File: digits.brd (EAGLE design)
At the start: 240.9 x 81 mm, 49 parts, among them IC1 STP16CP05 / STP16CPC26, IC2 STP16CP05 / STP16CPC26, IC3 ATMEGA32U4QFN, IC4 ATMEGA32U4TQFP-44, J1 POWER_JACKPTH_LOCK, J2 ACCESSORY, X1 CRYSTALHC49

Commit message: added boost converter
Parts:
- added C11, C12: 0.1uF, SparkFun-Capacitors:0805
- added C13: 100uF, SparkFun-Capacitors:PANASONIC_D
- added C14: 470uF, SparkFun-Capacitors:PANASONIC_D
- added C15: 470pF, SparkFun-Capacitors:0805
- added D3: BYV10-40, diode:MELF-MLL41
- added IC6: 7805DT, adafruit:TO252
- added L2: 200uH, Livestream:SRN1060
- added R13: 0.33R, SparkFun-Resistors:0805
- added R14: 1.2k, SparkFun-Resistors:0805
- added R15: 3.6k, SparkFun-Resistors:0805
- added U1: MC34063SMD, SparkFun-PowerIC:SO08
- C7, C8, C9: value 100nF -> 0.1uF
- moved J2 85.1 mm to (124.5, 100.8)
- moved U$1 48.0 mm to (69.5, 30.1)
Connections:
- removed net D13: J2.18
- removed net MOSI: IC1.2, JP3.3
- removed net PD0: JP3.7, JP6.4
- removed net PD1: JP3.8, JP6.3
- removed net SCK: IC1.3, IC2.3, JP3.4, JP6.7
- new net N$13: R13.1, U1.1, U1.7, U1.8
- new net N$14: D3.C, L2.P$1, U1.2
- new net N$15: C15.2, U1.3
- new net N$16: R14.2, R15.1, U1.5
- new net VCCLEDS: C14.+, L2.P$2, R15.2, T1.2, T2.2, T3.2, T4.2, T5.2
- net BLANK: no longer JP3.6, JP6.5
- net D0/RX: now also JP3.3, JP6.8
- net D1/TX: now also JP3.4, JP6.7
- net D2/SDA: now also JP3.5, JP6.6
- net D3/SCL: now also JP3.6, JP6.5
- net D4/MOSI: now also IC1.2
- net D6/SCK: now also IC1.3, IC2.3
- net D7: now also JP3.7, JP6.4
- net D8: now also JP3.8, JP6.3
- net GND: now also C11.2, C12.2, C13.-, C14.-, C15.1, D3.A, IC6.3, R14.1, U1.4
- net LATCH: no longer JP3.5, JP6.6
- net SDO2: no longer JP6.8
- net VCC: now also C13.+, R13.2, U1.6; no longer C1.1, C2.1, IC1.24, IC2.24, J2.1, J2.2, JP3.1, JP3.2, JP6.10, JP6.9, T1.2, T2.2, T3.2, T4.2, T5.2
- net VCC5V: now also C1.1, C12.1, C2.1, IC1.24, IC2.24, IC6.2, J2.1, J2.2, JP3.1, JP6.10
- net VCC9V: now also C11.1, IC6.1, JP3.2, JP6.9
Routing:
- net VCC: track 572.5 -> 0.00 mm, vias 10 -> 0
- net VCC5V: track 71.9 -> 621.6 mm, vias 6 -> 16
- net BLANK: track 347.1 -> 17.3 mm, vias 6 -> 1
- net PD0: track 265.0 -> 0.00 mm, vias 9 -> 0
- net PD1: track 240.4 -> 0.00 mm, vias 3 -> 0
- net LATCH: track 306.4 -> 66.6 mm, vias 8 -> 3
- net SCK: track 210.4 -> 0.00 mm, vias 7 -> 0
- net MOSI: track 140.8 -> 0.00 mm, vias 6 -> 0
- net D13: track 112.6 -> 0.00 mm, vias 3 -> 0
- net D7: track 96.0 -> 194.7 mm, vias 1 -> 5
- net D9: track 101.2 -> 8.00 mm, vias 3 -> 0
- net D5/MISO: track 127.5 -> 53.2 mm, vias 2 -> 1
- net D12: track 65.7 -> 2.91 mm, vias 2 -> 0
- net D11: track 64.4 -> 6.59 mm, vias 4 -> 2
- net D1/TX: track 61.3 -> 10.6 mm, vias 2 -> 0
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
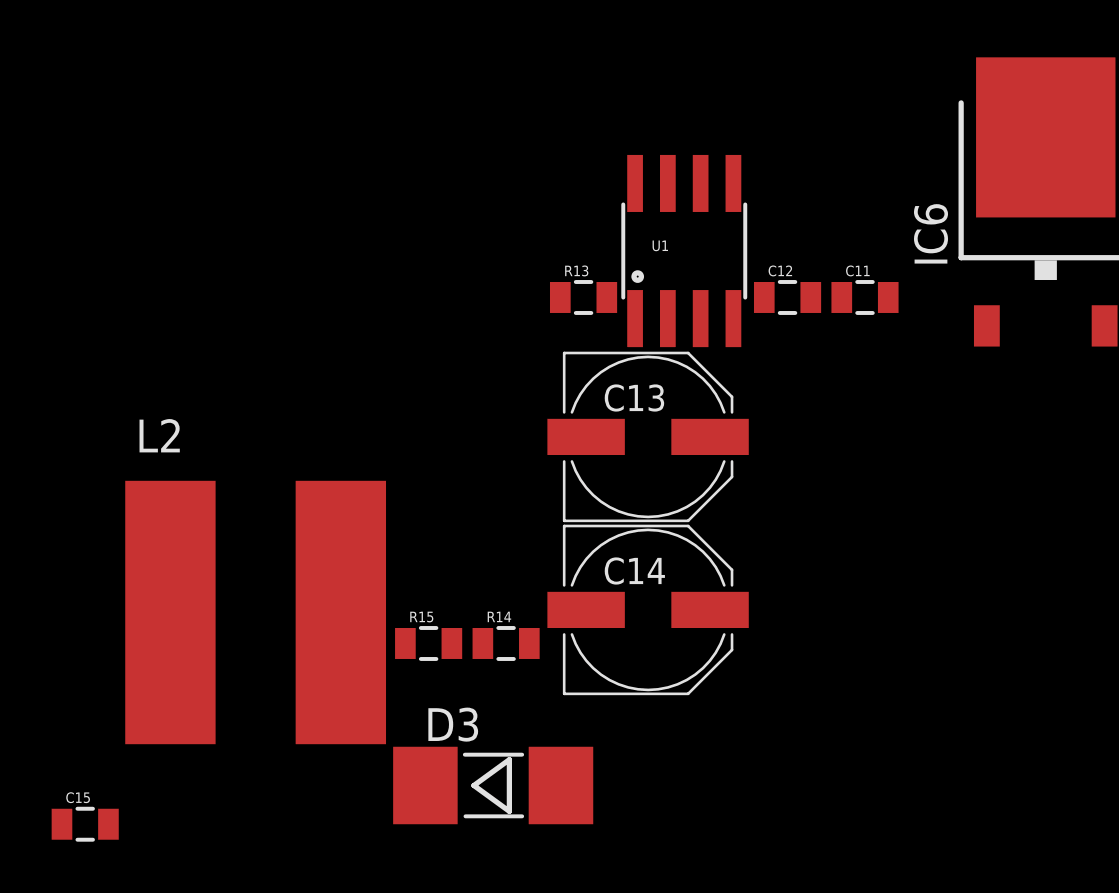
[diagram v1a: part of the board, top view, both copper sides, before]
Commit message: added tssop shifter, pololu boost
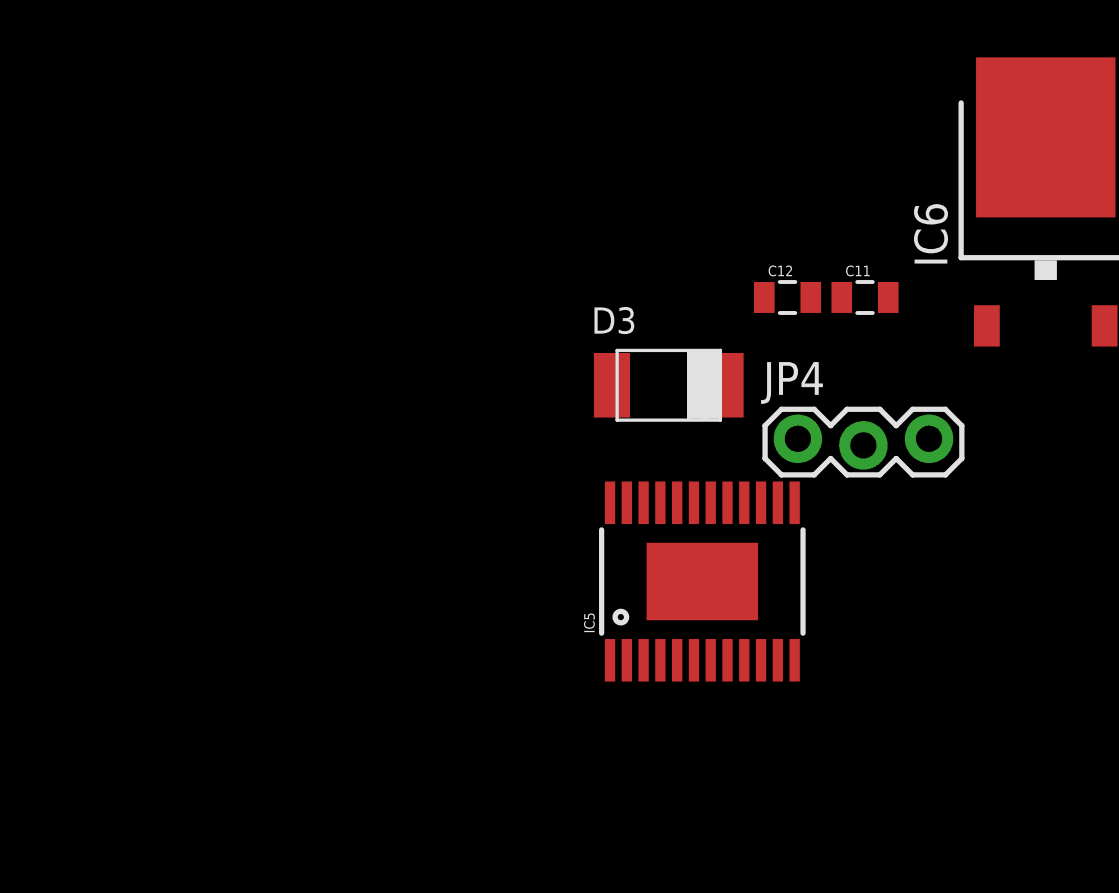
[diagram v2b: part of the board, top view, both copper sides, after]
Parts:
- removed C13: 100uF, SparkFun-Capacitors:PANASONIC_D
- removed C14: 470uF, SparkFun-Capacitors:PANASONIC_D
- removed C15: 470pF, SparkFun-Capacitors:0805
- removed L2: 200uH, Livestream:SRN1060
- removed R13: 0.33R, SparkFun-Resistors:0805
- removed R14: 1.2k, SparkFun-Resistors:0805
- removed R15: 3.6k, SparkFun-Resistors:0805
- removed U1: MC34063SMD, SparkFun-PowerIC:SO08
- added IC5: STP16CP05, digits:TSSOP-24
- added JP4: (no value), SparkFun-Connectors:1X03_LOCK
- D3: value BYV10-40 -> PMEG3030EP; device diode:MELF-MLL41 -> digits:SOD-128
- moved D3 16.9 mm to (-47.1, -6.40)
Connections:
- removed net N$14: D3.C, L2.P$1, U1.2
- removed net N$15: C15.2, U1.3
- removed net N$16: R14.2, R15.1, U1.5
- removed net VCC: C13.+, R13.2, U$1.24, U1.6
- removed net VCCLEDS: C14.+, L2.P$2, R15.2, T1.2, T2.2, T3.2, T4.2, T5.2
- net GND: now also JP4.2; no longer C13.-, C14.-, C15.1, D3.A, R14.1, U1.4
- net N$13: now also D3.A, JP4.3; no longer R13.1, U1.1, U1.7, U1.8
- net VCC5V: now also JP4.1
- net VCC9V: now also D3.C, T1.2, T2.2, T3.2, T4.2, T5.2, U$1.24

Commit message: started rerouting
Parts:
- removed IC5: STP16CP05, digits:TSSOP-24
- moved D3 95.5 mm to (44.6, 20.2), flipped to the bottom, turned to 90 degrees
- moved JP4 85.0 mm to (39.6, 14.8), flipped to the bottom, turned to 180 degrees
- moved T2 1.21 mm to (56.6, 5.50), turned to 270 degrees
- moved T3 1.20 mm to (105.7, 5.50), turned to 270 degrees
- moved T5 1.17 mm to (202.0, 5.50), turned to 270 degrees
- moved T4 1.08 mm to (153.6, 5.50), turned to 270 degrees
- moved T1 1.08 mm to (9.00, 5.40), turned to 270 degrees
- flipped C11 to the bottom
- flipped C12 to the bottom
- turned D1 to 180 degrees
- flipped IC6 to the bottom
- flipped R10 to the bottom
- flipped R11 to the bottom
- flipped R12 to the bottom
- flipped R7 to the bottom
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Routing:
- net VCC5V: track 621.6 -> 111.5 mm, vias 16 -> 6
- net D7: track 194.7 -> 50.1 mm, vias 5 -> 3
- net GATE3: track 163.3 -> 43.2 mm
- net GATE4: track 200.0 -> 81.0 mm
- net GATE2: track 118.3 -> 11.6 mm, vias 4 -> 2
- net VCC9V: track 0.00 -> 69.2 mm, vias 0 -> 1
- net ROW0: track 97.0 -> 41.3 mm
- net GATE1: track 65.2 -> 33.1 mm
- net GATE0: track 74.8 -> 64.9 mm
- net N$13: track 0.00 -> 3.36 mm
- net N$3: track 11.0 -> 13.2 mm

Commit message: layout, chronodot
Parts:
- added IC5: CHRONODOT, digits:CHRONODOT
- added R13, R14, R15, R16, R17: 910R, SparkFun-Resistors:0805
- added R18: 10k, SparkFun-Resistors:0805
- added SJ1: SOLDERJUMPERNO, SparkFun-Passives:SJ_2S-NO
- R10, R11, R12, R7, R9: value 1k -> 910R
- moved R12 212.0 mm to (198.4, 4.20), turned to 180 degrees
- moved R11 160.9 mm to (150.2, 4.50), turned to 180 degrees
- moved R10 109.9 mm to (102.1, 4.50), turned to 180 degrees
- moved J2 67.4 mm to (107.3, 35.6)
- moved R9 57.7 mm to (52.7, 4.50), turned to 180 degrees
- moved R7 10.1 mm to (5.40, 4.40), turned to 180 degrees
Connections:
- removed net D7/PRESENCE: IC3.33, IC4.33, J2.23, U$1.20
- removed net SDO2: IC2.22
- new net N$14: IC5.7, R18.2, SJ1.2
- new net PRESENCE: IC3.33, IC4.33, J2.23
- net D2/SDA: now also IC5.4
- net D3/SCL: now also IC5.3
- net D7: now also SJ1.1, U$1.20
- net GND: now also IC5.1
- net N$10: now also R14.1
- net N$11: now also R15.1
- net N$12: now also R17.1
- net N$8: now also R16.1
- net N$9: now also R13.1
- net VCC5V: now also IC5.2, R18.1
- net VCC9V: now also R13.2, R14.2, R15.2, R16.2, R17.2
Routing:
- net D7: track 50.1 -> 281.4 mm, vias 3 -> 10
- net VCC9V: track 69.2 -> 278.9 mm, vias 1 -> 10
- net D0/RX: track 0.00 -> 184.9 mm, vias 0 -> 3
- net D2/SDA: track 2.58 -> 176.0 mm, vias 0 -> 2
- net D3/SCL: track 0.00 -> 157.3 mm, vias 0 -> 5
- net D1/TX: track 10.6 -> 163.0 mm, vias 0 -> 2
- net GATE4: track 81.0 -> 229.1 mm, vias 4 -> 5
- net GATE3: track 43.2 -> 189.4 mm, vias 4 -> 2
- net LATCH: track 66.6 -> 187.9 mm, vias 3 -> 6
- net D9: track 8.00 -> 127.3 mm, vias 0 -> 4
- net BLANK: track 17.3 -> 135.7 mm, vias 1 -> 3
- net D4/MOSI: track 13.8 -> 126.8 mm, vias 1 -> 3
- net GATE2: track 11.6 -> 120.5 mm
- net D6/SCK: track 10.2 -> 113.2 mm, vias 1 -> 2
- net VCC5V: track 111.5 -> 213.8 mm, vias 6 -> 7
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
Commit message: more routing fun
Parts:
- added D4, D5: PMEG3030EP, digits:SOD-128
- moved C12 159.5 mm to (115.2, 21.0), turned to 270 degrees
- moved C11 156.0 mm to (115.2, 17.3), turned to 90 degrees
- moved IC6 156.0 mm to (122.4, 19.2), turned to 90 degrees
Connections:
- removed net RX: IC3.20, IC4.20
- removed net TX: IC3.21, IC4.21
- new net N$15: D5.A, U$1.1
- net D0/RX: now also IC3.20, IC4.20
- net D1/TX: now also IC3.21, IC4.21
- net VCC5V: now also D4.A, D4.C, D5.C, U$1.24; no longer U$1.1
- net VCC9V: no longer U$1.24
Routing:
- net D3/SCL: track 157.3 -> 337.9 mm, vias 5 -> 10
- net D2/SDA: track 176.0 -> 353.3 mm, vias 2 -> 4
- net D6/SCK: track 113.2 -> 250.0 mm, vias 2 -> 3
- net D8: track 126.6 -> 247.0 mm, vias 5 -> 7
- net VCC5V: track 213.8 -> 315.0 mm, vias 7 -> 8
- net D1/TX: track 163.0 -> 252.3 mm, vias 2 -> 6
- net D7: track 281.4 -> 362.1 mm
- net D0/RX: track 184.9 -> 263.3 mm, vias 3 -> 6
- net D5/MISO: track 96.2 -> 169.8 mm, vias 2 -> 3
- net A2: track 46.0 -> 93.0 mm, vias 1 -> 3
- net GATE0: track 81.9 -> 128.6 mm, vias 2 -> 4
- net A0: track 36.0 -> 82.6 mm, vias 1 -> 4
- net A1: track 41.3 -> 85.8 mm, vias 1 -> 4
- net BLANK: track 135.7 -> 175.5 mm, vias 3 -> 6
- net LATCH: track 187.9 -> 220.1 mm
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
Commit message: rerouting to put all reflowed components closer to the center
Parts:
- moved R18 233.8 mm to (176.4, 30.8), flipped to the bottom
- moved SJ1 227.7 mm to (172.9, 31.3), flipped to the bottom, turned to 270 degrees
- moved T5 92.1 mm to (110.0, 2.10)
- moved R12 90.7 mm to (107.8, -0.70)
- moved R17 90.7 mm to (107.8, -2.60)
- moved C2 70.0 mm to (95.0, 33.1), turned to 90 degrees
- moved R2 68.9 mm to (98.2, 19.8), turned to 180 degrees
- moved C1 66.8 mm to (95.0, 53.5)
- moved R1 66.7 mm to (98.2, 40.4), turned to 180 degrees
- moved IC1 65.8 mm to (104.2, 48.8)
- moved IC2 65.8 mm to (104.2, 28.4)
- moved T4 48.0 mm to (105.7, 2.00)
- moved R11 46.8 mm to (103.7, -0.70)
- moved R16 46.8 mm to (103.7, -2.60)
- moved J2 42.3 mm to (149.6, 35.9)
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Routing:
- net D12: track 2.65 -> 201.4 mm, vias 0 -> 2
- net PRESENCE: track 3.02 -> 160.5 mm, vias 0 -> 4
- net VCC5V: track 315.0 -> 179.8 mm
- net D0/RX: track 263.3 -> 147.6 mm, vias 6 -> 4
- net ROW4: track 87.1 -> 188.5 mm
- net GATE4: track 228.8 -> 145.4 mm, vias 7 -> 5
- net D3/SCL: track 337.9 -> 283.7 mm, vias 10 -> 6
- net A1: track 85.8 -> 138.7 mm, vias 4 -> 5
- net LATCH: track 220.1 -> 167.5 mm, vias 6 -> 5
- net D2/SDA: track 353.3 -> 303.6 mm, vias 4 -> 6
- net A0: track 82.6 -> 132.2 mm, vias 4 -> 6
- net A2: track 93.0 -> 142.2 mm, vias 3 -> 4
- net D5/MISO: track 169.8 -> 215.9 mm, vias 3 -> 4
- net GATE3: track 189.4 -> 144.3 mm, vias 4 -> 2
- net ROW3: track 100.2 -> 56.0 mm, vias 4 -> 1
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
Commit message: finished relayout
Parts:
- added CORE: Spark Core, Spark:SPARK_CORE
- added U$2: FIDUCIAL, adafruit:FIDUCIAL_1MM
- SJ1: value SOLDERJUMPERNO -> SQW
- U$1: value SPARK_CORECORE -> FIDUCIAL; device Spark:SPARK_CORE -> adafruit:FIDUCIAL_1MM
- moved R18 80.4 mm to (105.4, 68.5), turned to 180 degrees
- moved U$1 77.9 mm to (2.00, 69.0), turned to 0 degrees
- moved C11 22.6 mm to (137.8, 16.9)
- moved D4 22.4 mm to (139.4, 38.4), turned to 90 degrees
- moved C12 20.0 mm to (135.2, 21.5), turned to 90 degrees
- moved IC6 19.1 mm to (141.0, 17.0), turned to 90 degrees
- moved SJ1 2.45 mm to (172.4, 33.7), turned to 180 degrees
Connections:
- new net N$16: C12.1, D4.A, IC6.2
- net A0: now also CORE.12; no longer U$1.12
- net A1: now also CORE.11; no longer U$1.11
- net A2: now also CORE.10; no longer U$1.10
- net BLANK: now also CORE.6; no longer U$1.6
- net D0/RX: now also CORE.4; no longer U$1.4
- net D1/TX: now also CORE.3; no longer U$1.3
- net D2/SDA: now also CORE.13; no longer U$1.13
- net D3/SCL: now also CORE.14; no longer U$1.14
- net D4/MOSI: now also CORE.7; no longer U$1.7
- net D5/MISO: now also CORE.8; no longer U$1.8
- net D6/SCK: now also CORE.9; no longer U$1.9
- net D7: now also CORE.20; no longer U$1.20
- net GATE0: now also CORE.15; no longer U$1.15
- net GATE1: now also CORE.16; no longer U$1.16
- net GATE2: now also CORE.17; no longer U$1.17
- net GATE3: now also CORE.18; no longer U$1.18
- net GATE4: now also CORE.19; no longer U$1.19
- net GND: now also CORE.2, CORE.21; no longer U$1.2, U$1.21
- net LATCH: now also CORE.5; no longer U$1.5
- net N$15: now also CORE.1; no longer U$1.1
- net VCC5V: now also CORE.24; no longer C12.1, D4.A, IC6.2, U$1.24
- net VDDA: now also CORE.22; no longer U$1.22
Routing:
- net VCC5V: track 179.8 -> 462.4 mm, vias 8 -> 19
- net N$14: track 0.00 -> 116.9 mm, vias 0 -> 2
- net D4/MOSI: track 122.3 -> 227.5 mm, vias 4 -> 6
- net VCC9V: track 272.8 -> 375.8 mm, vias 9 -> 14
- net D0/RX: track 147.6 -> 241.4 mm, vias 4 -> 8
- net ROW3: track 56.0 -> 140.3 mm, vias 1 -> 3
- net D3/SCL: track 283.7 -> 347.9 mm, vias 6 -> 8
- net ROW0: track 41.7 -> 98.2 mm, vias 2 -> 4
- net ROW2: track 39.7 -> 92.1 mm, vias 1 -> 3
- net D2/SDA: track 303.6 -> 354.9 mm
- net N$16: track 0.00 -> 25.6 mm
- net COL-E: track 319.4 -> 297.2 mm, vias 6 -> 5
- net COL-C: track 288.5 -> 277.7 mm, vias 6 -> 5
- net GND: track 54.5 -> 62.1 mm, vias 14 -> 79
- net D7: track 343.7 -> 351.1 mm, vias 10 -> 12
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- added copper zone on layer 16, net GND
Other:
- outline, holes or cut-outs redrawn
- board text added: "D10"
- board text added: "D4"
- board text added: "D5"
- board text added: "D9"
- board text removed: "2014 PloverElectric.com"
- board text removed: "A4"
- board text removed: "A5"
- board text removed: "CS"
- board text removed: "D13"
- board text removed: "D14"
- board text removed: "D15"
- board text removed: "D16"
- board text removed: "D17"
- board text removed: "Digits"
- board text removed: "Plover Electric"
- board text removed: "RDY"

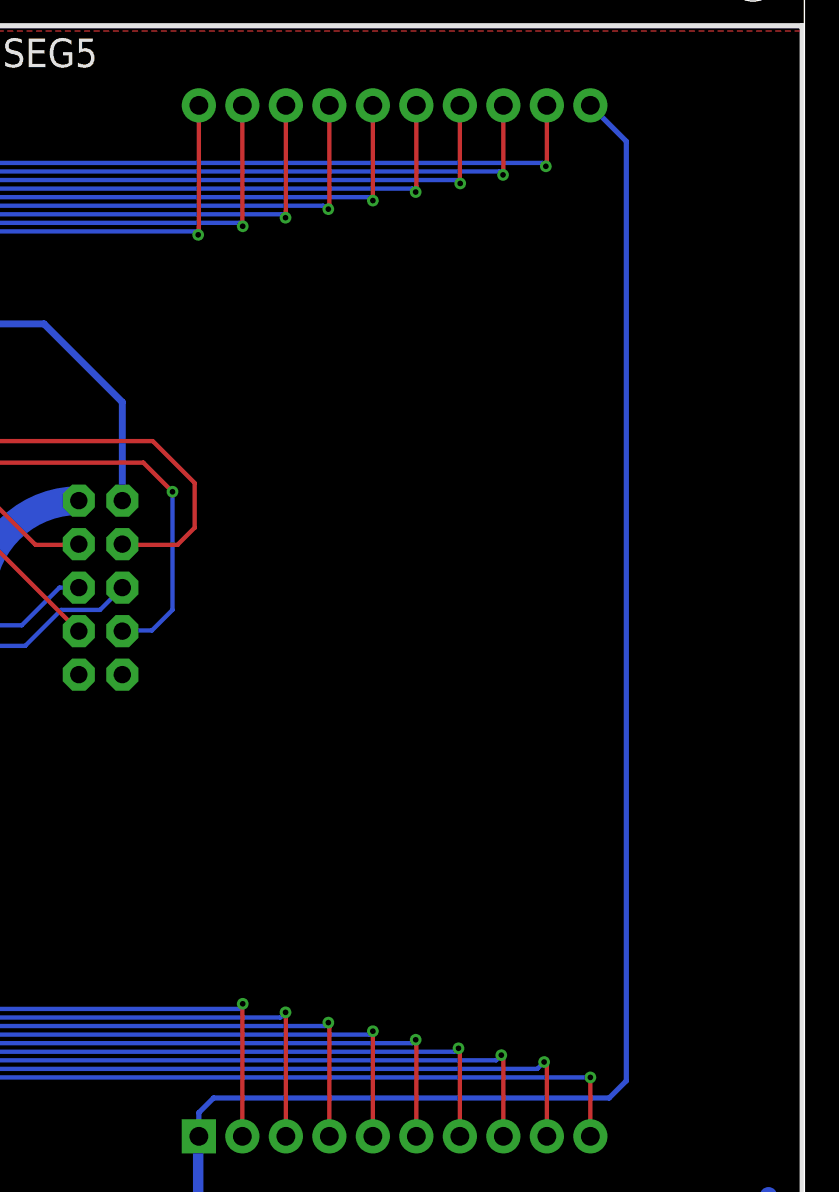
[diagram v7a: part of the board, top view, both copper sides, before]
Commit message: added bird logo
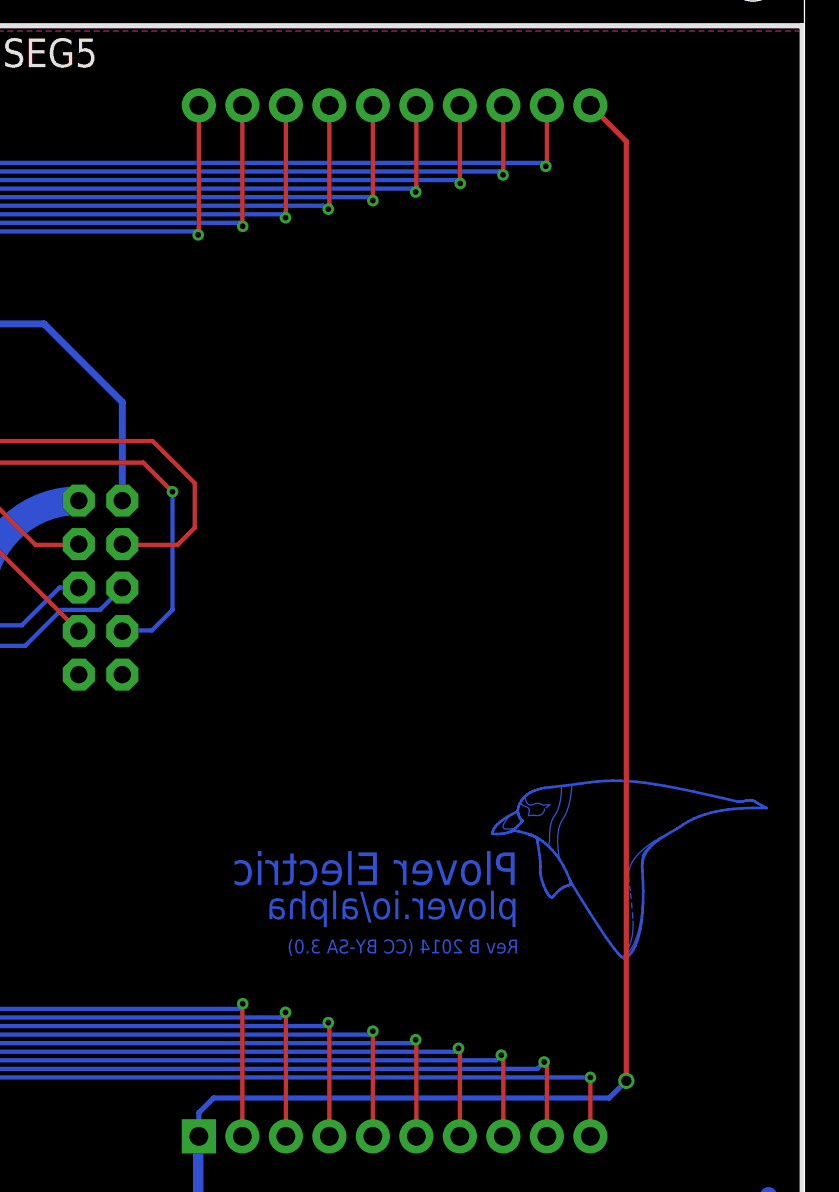
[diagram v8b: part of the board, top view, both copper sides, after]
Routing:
- net BIRD1: track 0.00 -> 50.8 mm
- net ROW4: vias 0 -> 1
- added copper zone on layer 16, net BIRD1
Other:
- board text added: "Plover Electric"
- board text added: "Rev B 2014 (CC BY-SA 3.0)"
- board text added: "plover.io/alpha"
- board text removed: "Rev 0.1 July 12 2014"
